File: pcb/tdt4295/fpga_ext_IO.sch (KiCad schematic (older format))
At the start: 37 parts

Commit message: Add digikey footprints, implement (some) capacitor footprints in schematic
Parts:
- J? (x2): footprint (none) -> Connector_PinHeader_1.00mm:PinHeader_2x08_P1.00mm_Vertical
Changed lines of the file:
@@
 F 0 "J?" H 2600 1867 50  0000 C CNN
 F 1 "Conn_02x08_Odd_Even" H 2600 1776 50  0000 C CNN
-F 2 "" H 2550 1350 50  0001 C CNN
+F 2 "Connector_PinHeader_1.00mm:PinHeader_2x08_P1.00mm_Vertical" H 2550 1350 50  0001 C CNN
 F 3 "~" H 2550 1350 50  0001 C CNN
 	1    2550 1350
@@
 F 0 "J?" H 2600 3367 50  0000 C CNN
 F 1 "Conn_02x08_Odd_Even" H 2600 3276 50  0000 C CNN
-F 2 "" H 2550 2850 50  0001 C CNN
+F 2 "Connector_PinHeader_1.00mm:PinHeader_2x08_P1.00mm_Vertical" H 2550 2850 50  0001 C CNN
 F 3 "~" H 2550 2850 50  0001 C CNN
 	1    2550 2850

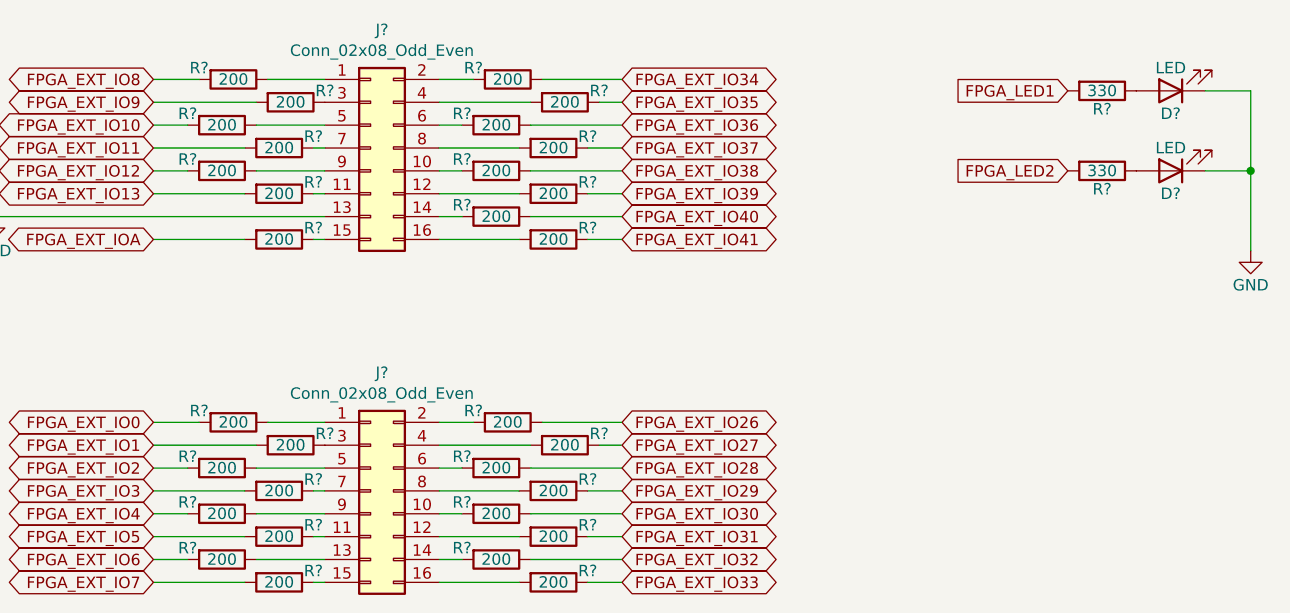
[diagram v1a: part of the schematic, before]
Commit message: associate symbol components
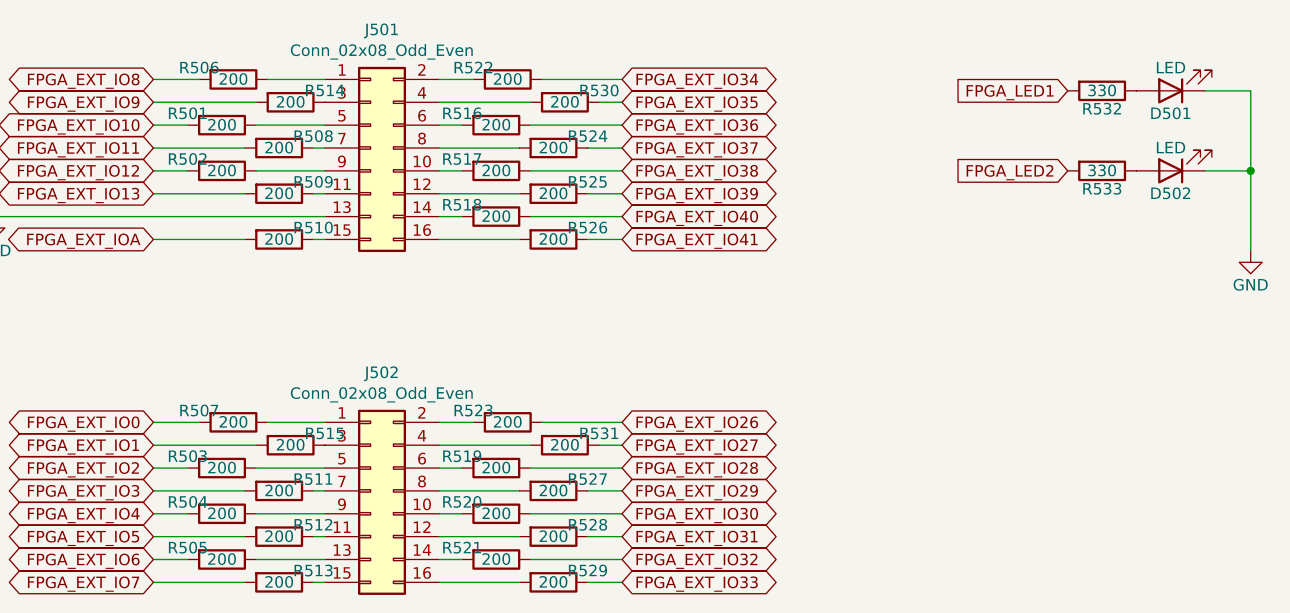
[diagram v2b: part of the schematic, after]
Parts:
- D501, D502: renamed from D?; footprint (none) -> Diode_SMD:D_0805_2012Metric_Pad1.15x1.40mm_HandSolder
- gave numbers to parts that had none: 35
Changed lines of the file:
@@
 $EndDescr
 $Comp
-L Connector_Generic:Conn_02x08_Odd_Even J?
+L Connector_Generic:Conn_02x08_Odd_Even J501
 U 1 1 6155E5DE
 P 2550 1350
-F 0 "J?" H 2600 1867 50  0000 C CNN
+F 0 "J501" H 2600 1867 50  0000 C CNN
 F 1 "Conn_02x08_Odd_Even" H 2600 1776 50  0000 C CNN
 F 2 "Connector_PinHeader_1.00mm:PinHeader_2x08_P1.00mm_Vertical" H 2550 1350 50  0001 C CNN
@@
 FPGA_EXT_IO41
 $Comp
-L Device:R R?
+L Device:R R522
 U 1 1 61562485
 P 3150 1050
-F 0 "R?" V 3100 900 50  0000 C CNN
+F 0 "R522" V 3100 900 50  0000 C CNN
 F 1 "200" V 3150 1050 50  0000 C CNN
 F 2 "" V 3080 1050 50  0001 C CNN
@@
 $EndComp
 $Comp
-L Device:R R?
+L Device:R R530
 U 1 1 61562FEB
 P 3400 1150
-F 0 "R?" V 3350 1300 50  0000 C CNN
+F 0 "R530" V 3350 1300 50  0000 C CNN
 F 1 "200" V 3400 1150 50  0000 C CNN
 F 2 "" V 3330 1150 50  0001 C CNN
@@
 $EndComp
 $Comp
-L Device:R R?
+L Device:R R516
 U 1 1 61564BDE
 P 3100 1250
-F 0 "R?" V 3050 1100 50  0000 C CNN
+F 0 "R516" V 3050 1100 50  0000 C CNN
 F 1 "200" V 3100 1250 50  0000 C CNN
 F 2 "" V 3030 1250 50  0001 C CNN
@@
 $EndComp
 $Comp
-L Device:R R?
+L Device:R R524
 U 1 1 61564BE4
 P 3350 1350
-F 0 "R?" V 3300 1500 50  0000 C CNN
+F 0 "R524" V 3300 1500 50  0000 C CNN
 F 1 "200" V 3350 1350 50  0000 C CNN
 F 2 "" V 3280 1350 50  0001 C CNN
@@
 $EndComp
 $Comp
-L Device:R R?
+L Device:R R517
 U 1 1 6156547C
 P 3100 1450
-F 0 "R?" V 3050 1300 50  0000 C CNN
+F 0 "R517" V 3050 1300 50  0000 C CNN
 F 1 "200" V 3100 1450 50  0000 C CNN
 F 2 "" V 3030 1450 50  0001 C CNN
@@
 $EndComp
 $Comp
-L Device:R R?
+L Device:R R525
 U 1 1 61565482
 P 3350 1550
-F 0 "R?" V 3300 1700 50  0000 C CNN
+F 0 "R525" V 3300 1700 50  0000 C CNN
 F 1 "200" V 3350 1550 50  0000 C CNN
 F 2 "" V 3280 1550 50  0001 C CNN
@@
 $EndComp
 $Comp
-L Device:R R?
+L Device:R R518
 U 1 1 61565AF0
 P 3100 1650
-F 0 "R?" V 3050 1500 50  0000 C CNN
+F 0 "R518" V 3050 1500 50  0000 C CNN
 F 1 "200" V 3100 1650 50  0000 C CNN
 F 2 "" V 3030 1650 50  0001 C CNN
@@
 $EndComp
 $Comp
-L Device:R R?
+L Device:R R526
 U 1 1 61565AF6
 P 3350 1750
-F 0 "R?" V 3300 1900 50  0000 C CNN
+F 0 "R526" V 3300 1900 50  0000 C CNN
 F 1 "200" V 3350 1750 50  0000 C CNN
 F 2 "" V 3280 1750 50  0001 C CNN
@@
 $EndComp
 $Comp
-L Device:R R?
+L Device:R R506
 U 1 1 6156B3F5
 P 1950 1050
-F 0 "R?" V 1900 900 50  0000 C CNN
+F 0 "R506" V 1900 900 50  0000 C CNN
 F 1 "200" V 1950 1050 50  0000 C CNN
 F 2 "" V 1880 1050 50  0001 C CNN
@@
 $EndComp
 $Comp
-L Device:R R?
+L Device:R R514
 U 1 1 6156B3FB
 P 2200 1150
-F 0 "R?" V 2150 1300 50  0000 C CNN
+F 0 "R514" V 2150 1300 50  0000 C CNN
 F 1 "200" V 2200 1150 50  0000 C CNN
 F 2 "" V 2130 1150 50  0001 C CNN
@@
 $EndComp
 $Comp
-L Device:R R?
+L Device:R R501
 U 1 1 6156B401
 P 1900 1250
-F 0 "R?" V 1850 1100 50  0000 C CNN
+F 0 "R501" V 1850 1100 50  0000 C CNN
 F 1 "200" V 1900 1250 50  0000 C CNN
 F 2 "" V 1830 1250 50  0001 C CNN
@@
 $EndComp
 $Comp
-L Device:R R?
+L Device:R R508
 U 1 1 6156B407
 P 2150 1350
-F 0 "R?" V 2100 1500 50  0000 C CNN
+F 0 "R508" V 2100 1500 50  0000 C CNN
 F 1 "200" V 2150 1350 50  0000 C CNN
 F 2 "" V 2080 1350 50  0001 C CNN
@@
 $EndComp
 $Comp
-L Device:R R?
+L Device:R R502
 U 1 1 6156B40D
 P 1900 1450
-F 0 "R?" V 1850 1300 50  0000 C CNN
+F 0 "R502" V 1850 1300 50  0000 C CNN
 F 1 "200" V 1900 1450 50  0000 C CNN
 F 2 "" V 1830 1450 50  0001 C CNN
@@
 $EndComp
 $Comp
-L Device:R R?
+L Device:R R509
 U 1 1 6156B413
 P 2150 1550
-F 0 "R?" V 2100 1700 50  0000 C CNN
+F 0 "R509" V 2100 1700 50  0000 C CNN
 F 1 "200" V 2150 1550 50  0000 C CNN
 F 2 "" V 2080 1550 50  0001 C CNN
@@
 $EndComp
 $Comp
-L Device:R R?
+L Device:R R510
 U 1 1 6156B41F
 P 2150 1750
-F 0 "R?" V 2100 1900 50  0000 C CNN
+F 0 "R510" V 2100 1900 50  0000 C CNN
 F 1 "200" V 2150 1750 50  0000 C CNN
 F 2 "" V 2080 1750 50  0001 C CNN
@@
 $EndComp
 $Comp
-L power:GND #PWR?
+L power:GND #PWR0501
 U 1 1 6156BA18
 P 900 1650
-F 0 "#PWR?" H 900 1400 50  0001 C CNN
+F 0 "#PWR0501" H 900 1400 50  0001 C CNN
 F 1 "GND" H 900 1500 50  0000 C CNN
 F 2 "" H 900 1650 50  0001 C CNN
@@
 	2350 1050 2100 1050
 $Comp
-L Connector_Generic:Conn_02x08_Odd_Even J?
+L Connector_Generic:Conn_02x08_Odd_Even J502
 U 1 1 61588030
 P 2550 2850
-F 0 "J?" H 2600 3367 50  0000 C CNN
+F 0 "J502" H 2600 3367 50  0000 C CNN
 F 1 "Conn_02x08_Odd_Even" H 2600 3276 50  0000 C CNN
 F 2 "Connector_PinHeader_1.00mm:PinHeader_2x08_P1.00mm_Vertical" H 2550 2850 50  0001 C CNN
@@
 FPGA_EXT_IO33
 $Comp
-L Device:R R?
+L Device:R R523
 U 1 1 61588045
 P 3150 2550
-F 0 "R?" V 3100 2400 50  0000 C CNN
+F 0 "R523" V 3100 2400 50  0000 C CNN
 F 1 "200" V 3150 2550 50  0000 C CNN
 F 2 "" V 3080 2550 50  0001 C CNN
@@
 $EndComp
 $Comp
-L Device:R R?
+L Device:R R531
 U 1 1 6158804B
 P 3400 2650
-F 0 "R?" V 3350 2800 50  0000 C CNN
+F 0 "R531" V 3350 2800 50  0000 C CNN
 F 1 "200" V 3400 2650 50  0000 C CNN
 F 2 "" V 3330 2650 50  0001 C CNN
@@
 $EndComp
 $Comp
-L Device:R R?
+L Device:R R519
 U 1 1 61588051
 P 3100 2750
-F 0 "R?" V 3050 2600 50  0000 C CNN
+F 0 "R519" V 3050 2600 50  0000 C CNN
 F 1 "200" V 3100 2750 50  0000 C CNN
 F 2 "" V 3030 2750 50  0001 C CNN
@@
 $EndComp
 $Comp
-L Device:R R?
+L Device:R R527
 U 1 1 61588057
 P 3350 2850
-F 0 "R?" V 3300 3000 50  0000 C CNN
+F 0 "R527" V 3300 3000 50  0000 C CNN
 F 1 "200" V 3350 2850 50  0000 C CNN
 F 2 "" V 3280 2850 50  0001 C CNN
@@
 $EndComp
 $Comp
-L Device:R R?
+L Device:R R520
 U 1 1 6158805D
 P 3100 2950
-F 0 "R?" V 3050 2800 50  0000 C CNN
+F 0 "R520" V 3050 2800 50  0000 C CNN
 F 1 "200" V 3100 2950 50  0000 C CNN
 F 2 "" V 3030 2950 50  0001 C CNN
@@
 $EndComp
 $Comp
-L Device:R R?
+L Device:R R528
 U 1 1 61588063
 P 3350 3050
-F 0 "R?" V 3300 3200 50  0000 C CNN
+F 0 "R528" V 3300 3200 50  0000 C CNN
 F 1 "200" V 3350 3050 50  0000 C CNN
 F 2 "" V 3280 3050 50  0001 C CNN
@@
 $EndComp
 $Comp
-L Device:R R?
+L Device:R R521
 U 1 1 61588069
 P 3100 3150
-F 0 "R?" V 3050 3000 50  0000 C CNN
+F 0 "R521" V 3050 3000 50  0000 C CNN
 F 1 "200" V 3100 3150 50  0000 C CNN
 F 2 "" V 3030 3150 50  0001 C CNN
@@
 $EndComp
 $Comp
-L Device:R R?
+L Device:R R529
 U 1 1 6158806F
 P 3350 3250
-F 0 "R?" V 3300 3400 50  0000 C CNN
+F 0 "R529" V 3300 3400 50  0000 C CNN
 F 1 "200" V 3350 3250 50  0000 C CNN
 F 2 "" V 3280 3250 50  0001 C CNN
@@
 $EndComp
 $Comp
-L Device:R R?
+L Device:R R507
 U 1 1 61588075
 P 1950 2550
-F 0 "R?" V 1900 2400 50  0000 C CNN
+F 0 "R507" V 1900 2400 50  0000 C CNN
 F 1 "200" V 1950 2550 50  0000 C CNN
 F 2 "" V 1880 2550 50  0001 C CNN
@@
 $EndComp
 $Comp
-L Device:R R?
+L Device:R R515
 U 1 1 6158807B
 P 2200 2650
-F 0 "R?" V 2150 2800 50  0000 C CNN
+F 0 "R515" V 2150 2800 50  0000 C CNN
 F 1 "200" V 2200 2650 50  0000 C CNN
 F 2 "" V 2130 2650 50  0001 C CNN
@@
 $EndComp
 $Comp
-L Device:R R?
+L Device:R R503
 U 1 1 61588081
 P 1900 2750
-F 0 "R?" V 1850 2600 50  0000 C CNN
+F 0 "R503" V 1850 2600 50  0000 C CNN
 F 1 "200" V 1900 2750 50  0000 C CNN
 F 2 "" V 1830 2750 50  0001 C CNN
@@
 $EndComp
 $Comp
-L Device:R R?
+L Device:R R511
 U 1 1 61588087
 P 2150 2850
-F 0 "R?" V 2100 3000 50  0000 C CNN
+F 0 "R511" V 2100 3000 50  0000 C CNN
 F 1 "200" V 2150 2850 50  0000 C CNN
 F 2 "" V 2080 2850 50  0001 C CNN
@@
 $EndComp
 $Comp
-L Device:R R?
+L Device:R R504
 U 1 1 6158808D
 P 1900 2950
-F 0 "R?" V 1850 2800 50  0000 C CNN
+F 0 "R504" V 1850 2800 50  0000 C CNN
 F 1 "200" V 1900 2950 50  0000 C CNN
 F 2 "" V 1830 2950 50  0001 C CNN
@@
 $EndComp
 $Comp
-L Device:R R?
+L Device:R R512
 U 1 1 61588093
 P 2150 3050
-F 0 "R?" V 2100 3200 50  0000 C CNN
+F 0 "R512" V 2100 3200 50  0000 C CNN
 F 1 "200" V 2150 3050 50  0000 C CNN
 F 2 "" V 2080 3050 50  0001 C CNN
@@
 $EndComp
 $Comp
-L Device:R R?
+L Device:R R513
 U 1 1 61588099
 P 2150 3250
-F 0 "R?" V 2100 3400 50  0000 C CNN
+F 0 "R513" V 2100 3400 50  0000 C CNN
 F 1 "200" V 2150 3250 50  0000 C CNN
 F 2 "" V 2080 3250 50  0001 C CNN
@@
 	2350 2550 2100 2550
 $Comp
-L Device:R R?
+L Device:R R505
 U 1 1 6158ADEF
 P 1900 3150
-F 0 "R?" V 1850 3000 50  0000 C CNN
+F 0 "R505" V 1850 3000 50  0000 C CNN
 F 1 "200" V 1900 3150 50  0000 C CNN
 F 2 "" V 1830 3150 50  0001 C CNN
@@
 	1750 3150 1600 3150
 $Comp
-L Device:LED D?
+L Device:LED D501
 U 1 1 615A011F
 P 6050 1100
-F 0 "D?" H 6050 1200 50  0000 C CNN
+F 0 "D501" H 6050 1200 50  0000 C CNN
 F 1 "LED" H 6050 1000 50  0000 C CNN
-F 2 "" H 6050 1100 50  0001 C CNN
+F 2 "Diode_SMD:D_0805_2012Metric_Pad1.15x1.40mm_HandSolder" H 6050 1100 50  0001 C CNN
 F 3 "~" H 6050 1100 50  0001 C CNN
 	1    6050 1100
@@
 $EndComp
 $Comp
-L Device:LED D?
+L Device:LED D502
 U 1 1 615A0ABC
 P 6050 1450
-F 0 "D?" H 6050 1550 50  0000 C CNN
+F 0 "D502" H 6050 1550 50  0000 C CNN
 F 1 "LED" H 6050 1350 50  0000 C CNN
-F 2 "" H 6050 1450 50  0001 C CNN
+F 2 "Diode_SMD:D_0805_2012Metric_Pad1.15x1.40mm_HandSolder" H 6050 1450 50  0001 C CNN
 F 3 "~" H 6050 1450 50  0001 C CNN
 	1    6050 1450
@@
 FPGA_LED2
 $Comp
-L Device:R R?
+L Device:R R532
 U 1 1 615A5F7F
 P 5750 1100
-F 0 "R?" V 5830 1100 50  0000 C CNN
+F 0 "R532" V 5830 1100 50  0000 C CNN
 F 1 "330" V 5750 1100 50  0000 C CNN
 F 2 "" V 5680 1100 50  0001 C CNN
@@
 $EndComp
 $Comp
-L Device:R R?
+L Device:R R533
 U 1 1 615A6B3B
 P 5750 1450
-F 0 "R?" V 5830 1450 50  0000 C CNN
+F 0 "R533" V 5830 1450 50  0000 C CNN
 F 1 "330" V 5750 1450 50  0000 C CNN
 F 2 "" V 5680 1450 50  0001 C CNN
@@
 	6400 1450 6400 1800
 $Comp
-L power:GND #PWR?
+L power:GND #PWR0502
 U 1 1 615AD66C
 P 6400 1800
-F 0 "#PWR?" H 6400 1550 50  0001 C CNN
+F 0 "#PWR0502" H 6400 1550 50  0001 C CNN
 F 1 "GND" H 6400 1650 50  0000 C CNN
 F 2 "" H 6400 1800 50  0001 C CNN

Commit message: Major restructuring of FPGA outputs
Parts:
- removed J501: Conn_02x08_Odd_Even, Connector_PinHeader_1.00mm:PinHeader_2x08_P1.00mm_Vertical, symbol Connector_Generic:Conn_02x08_Odd_Even
- removed R501, R502, R506, R508, R509, R510, R513, R514, R516, R517, R518, R522, R524, R525, R526, R529, R530: 200, symbol Device:R
- added D? (x2): LED, Diode_SMD:D_0805_2012Metric_Pad1.15x1.40mm_HandSolder, symbol Device:LED
- added J?: 5177802-9, CONN_5177802-9_TEC, symbol 5177802-9:5177802-9
- added R? (x3): 4k, symbol Device:R
- added R? (x3): 2k, symbol Device:R
- added R? (x6): 1k, symbol Device:R
- added R? (x2): 100, symbol Device:R
- added R? (x2): 330, symbol Device:R
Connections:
- net labels added: +3V3, FPGA_LED0, FPGA_LED3, VGA_B0, VGA_B1, VGA_B2, VGA_B3, VGA_G0, VGA_G1, VGA_G2, VGA_G3, VGA_HS, VGA_R0, VGA_R1, VGA_R2, VGA_R3, VGA_VS
- net labels removed: FPGA_EXT_IO26, FPGA_EXT_IO27, FPGA_EXT_IO28, FPGA_EXT_IO29, FPGA_EXT_IO30, FPGA_EXT_IO31, FPGA_EXT_IO32, FPGA_EXT_IO33, FPGA_EXT_IO34, FPGA_EXT_IO35, FPGA_EXT_IO36, FPGA_EXT_IO37, FPGA_EXT_IO38, FPGA_EXT_IO39, FPGA_EXT_IO40, FPGA_EXT_IO41, FPGA_EXT_IOA
- wire segments 65 -> 95
- no-connect marks 0 -> 4
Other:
- note added: "GPIO header"
- note added: "ICD15S13E6GX00LF maybe?\n"
- note added: "User LEDs"
- note added: "VGA output"
- moved on the sheet: D501, D502, J502, R503, R504, R505, R507, R511, R512, R515, R519, R520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

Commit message: associate (most) symbols with footprints
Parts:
- added U301, U302, U303, U304: NUP4114UCW1T2G, SOIC_W1T2G_ONS, symbol NUP4114UCW1T2G:NUP4114UCW1T2G
- R302, R304, R306, R312, R314, R316: renamed from R?; footprint (none) -> Resistor_SMD:R_0402_1005Metric_Pad0.72x0.64mm_HandSolder; Component name (none) -> RR0510P-102-D
- R307: renamed from R532; footprint (none) -> Resistor_SMD:R_0805_2012Metric_Pad1.20x1.40mm_HandSolder; Component name (none) -> RK73H2ATTD3300F
- R308: renamed from R533; footprint (none) -> Resistor_SMD:R_0805_2012Metric_Pad1.20x1.40mm_HandSolder; Component name (none) -> RK73H2ATTD3300F
- R309, R310: renamed from R?; footprint (none) -> Resistor_SMD:R_0805_2012Metric_Pad1.20x1.40mm_HandSolder; Component name (none) -> RK73H2ATTD3300F
- R311, R313, R315: renamed from R?; footprint (none) -> Resistor_SMD:R_1206_3216Metric_Pad1.30x1.75mm_HandSolder; Component name (none) -> RC1206FR-072KL
- R317, R318: renamed from R?; footprint (none) -> Resistor_SMD:R_0805_2012Metric_Pad1.20x1.40mm_HandSolder; Component name (none) -> TNPW0805100RBEEA
- R319: renamed from R503; footprint (none) -> Resistor_SMD:R_0805_2012Metric_Pad1.20x1.40mm_HandSolder; Component name (none) -> RNCF0805TKY200R
- R320: renamed from R504; footprint (none) -> Resistor_SMD:R_0805_2012Metric_Pad1.20x1.40mm_HandSolder; Component name (none) -> RNCF0805TKY200R
- R321: renamed from R505; footprint (none) -> Resistor_SMD:R_0805_2012Metric_Pad1.20x1.40mm_HandSolder; Component name (none) -> RNCF0805TKY200R
- R322: renamed from R507; footprint (none) -> Resistor_SMD:R_0805_2012Metric_Pad1.20x1.40mm_HandSolder; Component name (none) -> RNCF0805TKY200R
- R323: renamed from R511; footprint (none) -> Resistor_SMD:R_0805_2012Metric_Pad1.20x1.40mm_HandSolder; Component name (none) -> RNCF0805TKY200R
- R324: renamed from R512; footprint (none) -> Resistor_SMD:R_0805_2012Metric_Pad1.20x1.40mm_HandSolder; Component name (none) -> RNCF0805TKY200R
- R325: renamed from R515; footprint (none) -> Resistor_SMD:R_0805_2012Metric_Pad1.20x1.40mm_HandSolder; Component name (none) -> RNCF0805TKY200R
- R326: renamed from R519; footprint (none) -> Resistor_SMD:R_0805_2012Metric_Pad1.20x1.40mm_HandSolder; Component name (none) -> RNCF0805TKY200R
- R327: renamed from R520; footprint (none) -> Resistor_SMD:R_0805_2012Metric_Pad1.20x1.40mm_HandSolder; Component name (none) -> RNCF0805TKY200R
- R328: renamed from R521; footprint (none) -> Resistor_SMD:R_0805_2012Metric_Pad1.20x1.40mm_HandSolder; Component name (none) -> RNCF0805TKY200R
- R329: renamed from R523; footprint (none) -> Resistor_SMD:R_0805_2012Metric_Pad1.20x1.40mm_HandSolder; Component name (none) -> RNCF0805TKY200R
- R330: renamed from R527; footprint (none) -> Resistor_SMD:R_0805_2012Metric_Pad1.20x1.40mm_HandSolder; Component name (none) -> RNCF0805TKY200R
- R331: renamed from R528; footprint (none) -> Resistor_SMD:R_0805_2012Metric_Pad1.20x1.40mm_HandSolder; Component name (none) -> RNCF0805TKY200R
- R332: renamed from R531; footprint (none) -> Resistor_SMD:R_0805_2012Metric_Pad1.20x1.40mm_HandSolder; Component name (none) -> RNCF0805TKY200R
- gave numbers to parts that had none: 6
- renumbered D501 to D301, D502 to D302, J502 to J302
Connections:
- wire segments 95 -> 134
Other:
- note added: "GPIO header \nwith ESD protection"
- note removed: "GPIO header"
- moved on the sheet: J302, R319, R320, R321, R322, R323, R324, R325, R326, R327, R328, R329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

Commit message: add final footprints, tweak VGA output
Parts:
- removed J301: 5177802-9, CONN_5177802-9_TEC, symbol 5177802-9:5177802-9
- added C301: 1nF/250V, cap_8853522100131:8853522100131, symbol Device:C
- added J301: 618015330923, VGA_618015330923-footprint:618015330923, symbol Connector:DB15_Female_HighDensity_MountingHoles
- added R317: 1M, Resistor_SMD:R_0805_2012Metric_Pad1.20x1.40mm_HandSolder, symbol Device:R
- J302: footprint Connector_PinHeader_1.00mm:PinHeader_2x08_P1.00mm_Vertical -> Connector_PinHeader_2.54mm:PinHeader_2x08_P2.54mm_Vertical
- R301, R303, R305: footprint (none) -> Resistor_SMD:R_1206_3216Metric_Pad1.30x1.75mm_HandSolder; Component name (none) -> RN73R2BTTD4001B25
- U301, U302, U303, U304: footprint SOIC_W1T2G_ONS -> NUP4114UCW1T2G-footprint:NUP4114UCW1T2G
- renumbered R317 to R319, R319 to R320, R320 to R321, R321 to R322, R322 to R323, R323 to R324, R324 to R325, R325 to R326, R326 to R327, R327 to R328, R328 to R329, R329 to R330, R330 to R331, R331 to R332, R332 to R333
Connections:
- wire segments 134 -> 131
- no-connect marks 4 -> 5
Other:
- note removed: "ICD15S13E6GX00LF maybe?\n"
- moved on the sheet: R318, R319

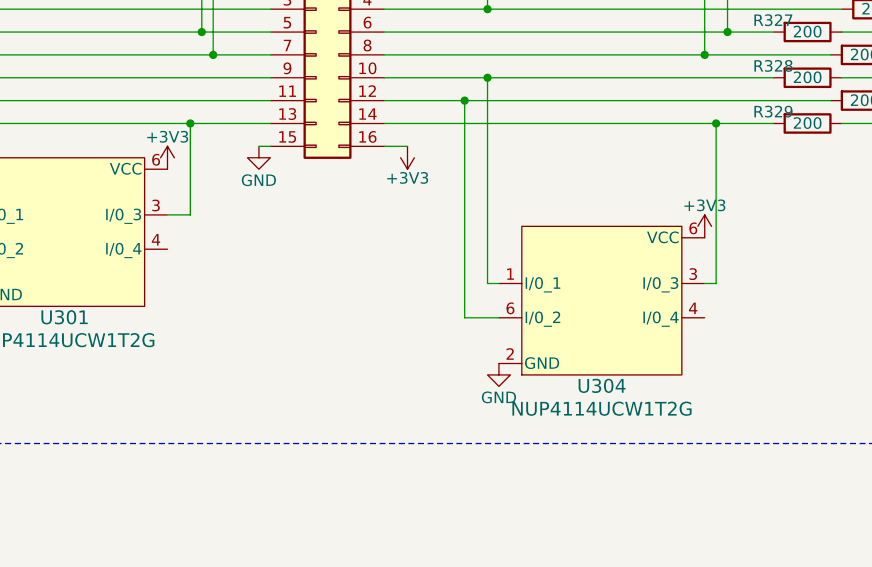
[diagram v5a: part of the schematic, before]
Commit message: Add some no connection symbols
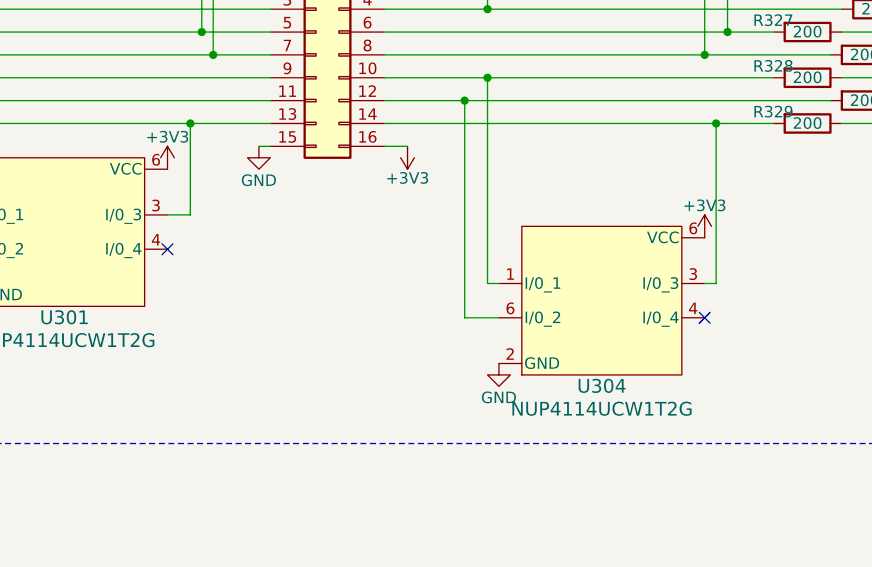
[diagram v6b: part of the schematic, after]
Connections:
- no-connect marks 5 -> 7
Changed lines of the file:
@@
 	1    0    0    -1
 $EndComp
+NoConn ~ 8450 3200
+NoConn ~ 6100 2900
 $EndSCHEMATC
